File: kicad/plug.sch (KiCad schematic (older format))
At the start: 14 parts, among them J1 74320-1004

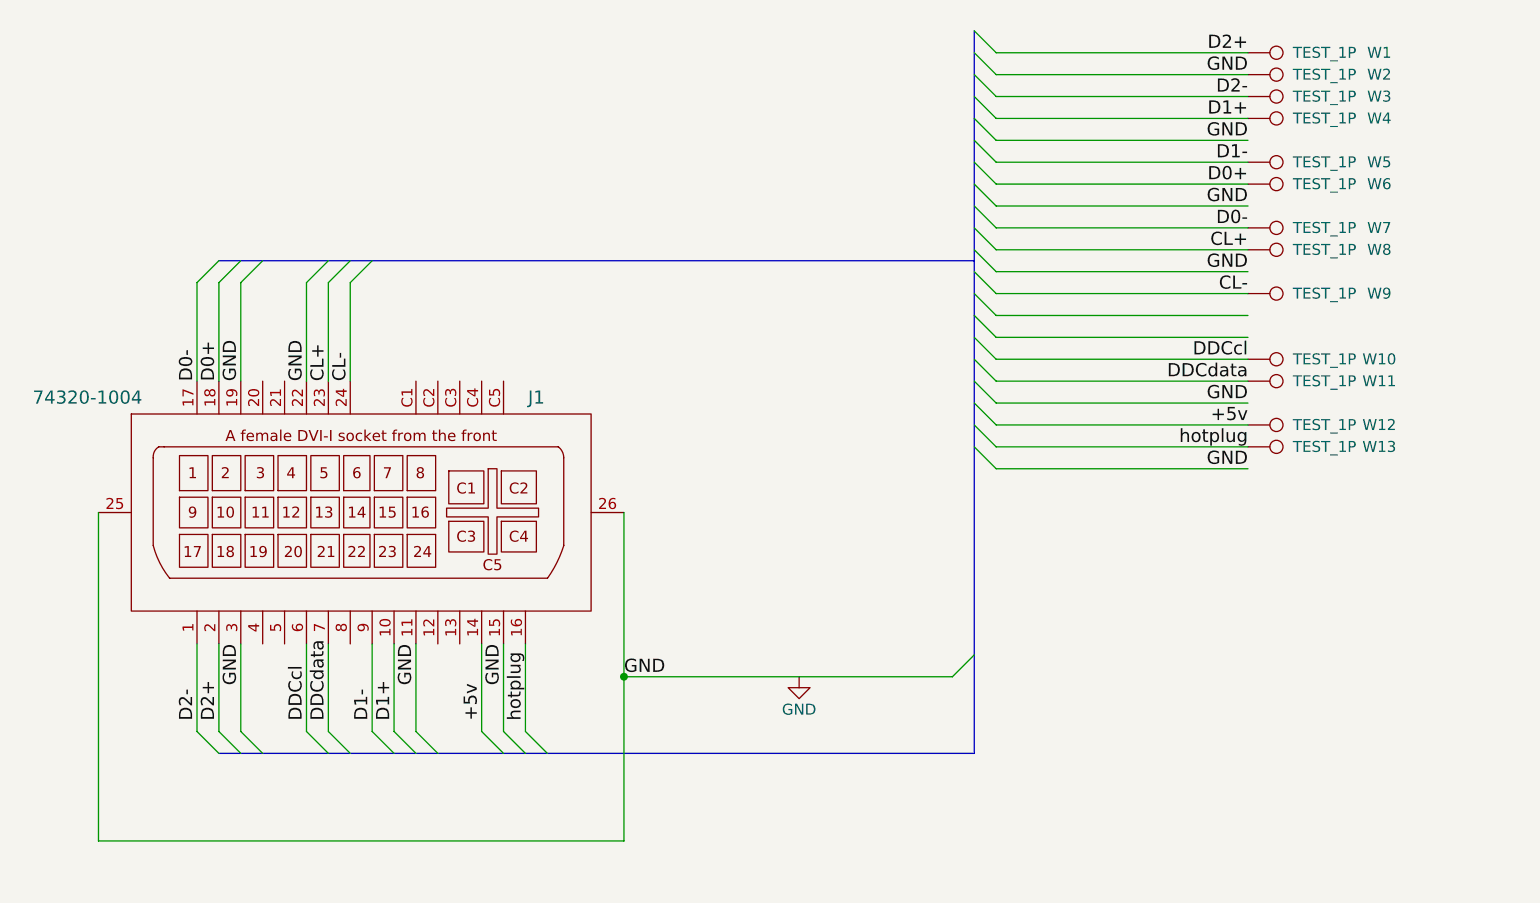
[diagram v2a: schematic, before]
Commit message: added pad footprint
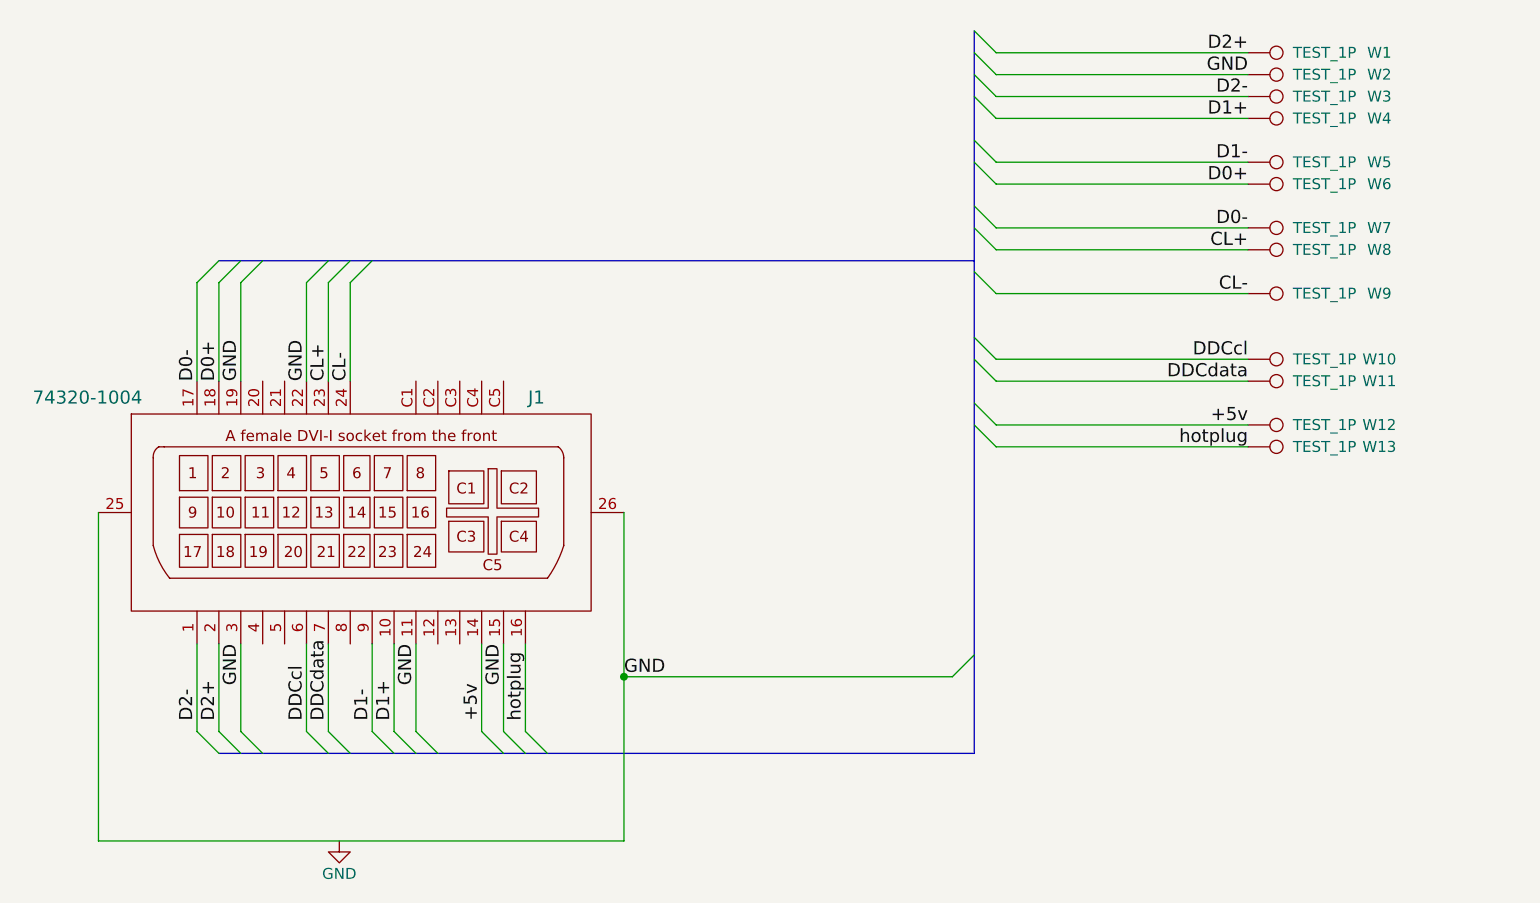
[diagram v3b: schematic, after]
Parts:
- W1, W10, W11, W12, W13, W2, W3, W4, W5, W6, W7, W8, W9: footprint Connectors:PINTST -> project:pad
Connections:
- wire segments 42 -> 35
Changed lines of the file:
@@
 	7700 3700 7800 3800
 Entry Wire Line
-	7700 3600 7800 3700
-Entry Wire Line
 	7700 3500 7800 3600
 Entry Wire Line
 	7700 3400 7800 3500
-Entry Wire Line
-	7700 3300 7800 3400
-Entry Wire Line
-	7700 3200 7800 3300
 Entry Wire Line
 	7700 3100 7800 3200
@@
 Text Label 4350 3600 1    60   ~ 0
 GND
-Entry Wire Line
-	7700 2700 7800 2800
-Text Label 8950 2800 2    60   ~ 0
-GND
-Entry Wire Line
-	7700 3000 7800 3100
-Text Label 8950 3100 2    60   ~ 0
-GND
 Wire Wire Line
 	6100 5700 3700 5700
@@
 	8950 3800 7800 3800
 Wire Wire Line
-	8950 3700 7800 3700
-Wire Wire Line
 	8950 3600 7800 3600
 Wire Wire Line
 	8950 3500 7800 3500
-Wire Wire Line
-	8950 3400 7800 3400
-Wire Wire Line
-	8950 3300 7800 3300
 Wire Wire Line
 	8950 3200 7800 3200
@@
 	4350 3600 4350 3150
 Wire Wire Line
-	7800 2800 8950 2800
-Wire Wire Line
-	7800 3100 8950 3100
-Wire Wire Line
 	4650 3600 4650 3150
 Entry Wire Line
@@
 	5150 5200 5250 5300
 Text Label 5150 4800 3    60   ~ 0
-GND
-Wire Wire Line
-	8950 2500 7800 2500
-Entry Wire Line
-	7700 2400 7800 2500
-Text Label 8950 2500 2    60   ~ 0
 GND
 Entry Wire Line
@@
 Connection ~ 6100 4950
 Text Label 6100 4950 0    60   ~ 0
-GND
-Entry Wire Line
-	7700 3900 7800 4000
-Wire Wire Line
-	7800 4000 8950 4000
-Text Label 8950 4000 2    60   ~ 0
-GND
-Text Label 8950 3700 2    60   ~ 0
 GND
 Entry Wire Line
@@
 F 0 "W1" V 8950 2700 50  0000 C CNN
 F 1 "TEST_1P" V 8950 2450 50  0000 C CNN
-F 2 "Connectors:PINTST" H 9150 2100 50  0001 C CNN
+F 2 "project:pad" H 9150 2100 50  0001 C CNN
 F 3 "" H 9150 2100 50  0000 C CNN
 	1    8950 2100
@@
 F 0 "W2" V 8950 2800 50  0000 C CNN
 F 1 "TEST_1P" V 8950 2550 50  0000 C CNN
-F 2 "Connectors:PINTST" H 9150 2200 50  0001 C CNN
+F 2 "project:pad" H 9150 2200 50  0001 C CNN
 F 3 "" H 9150 2200 50  0000 C CNN
 	1    8950 2200
@@
 F 0 "W3" V 8950 2900 50  0000 C CNN
 F 1 "TEST_1P" V 8950 2650 50  0000 C CNN
-F 2 "Connectors:PINTST" H 9150 2300 50  0001 C CNN
+F 2 "project:pad" H 9150 2300 50  0001 C CNN
 F 3 "" H 9150 2300 50  0000 C CNN
 	1    8950 2300
@@
 F 0 "W4" V 8950 3000 50  0000 C CNN
 F 1 "TEST_1P" V 8950 2750 50  0000 C CNN
-F 2 "Connectors:PINTST" H 9150 2400 50  0001 C CNN
+F 2 "project:pad" H 9150 2400 50  0001 C CNN
 F 3 "" H 9150 2400 50  0000 C CNN
 	1    8950 2400
@@
 F 0 "W5" V 8950 3200 50  0000 C CNN
 F 1 "TEST_1P" V 8950 2950 50  0000 C CNN
-F 2 "Connectors:PINTST" H 9150 2600 50  0001 C CNN
+F 2 "project:pad" H 9150 2600 50  0001 C CNN
 F 3 "" H 9150 2600 50  0000 C CNN
 	1    8950 2600
@@
 F 0 "W6" V 8950 3300 50  0000 C CNN
 F 1 "TEST_1P" V 8950 3050 50  0000 C CNN
-F 2 "Connectors:PINTST" H 9150 2700 50  0001 C CNN
+F 2 "project:pad" H 9150 2700 50  0001 C CNN
 F 3 "" H 9150 2700 50  0000 C CNN
 	1    8950 2700
@@
 F 0 "W7" V 8950 3500 50  0000 C CNN
 F 1 "TEST_1P" V 8950 3250 50  0000 C CNN
-F 2 "Connectors:PINTST" H 9150 2900 50  0001 C CNN
+F 2 "project:pad" H 9150 2900 50  0001 C CNN
 F 3 "" H 9150 2900 50  0000 C CNN
 	1    8950 2900
@@
 F 0 "W8" V 8950 3600 50  0000 C CNN
 F 1 "TEST_1P" V 8950 3350 50  0000 C CNN
-F 2 "Connectors:PINTST" H 9150 3000 50  0001 C CNN
+F 2 "project:pad" H 9150 3000 50  0001 C CNN
 F 3 "" H 9150 3000 50  0000 C CNN
 	1    8950 3000
@@
 F 0 "W9" V 8950 3800 50  0000 C CNN
 F 1 "TEST_1P" V 8950 3550 50  0000 C CNN
-F 2 "Connectors:PINTST" H 9150 3200 50  0001 C CNN
+F 2 "project:pad" H 9150 3200 50  0001 C CNN
 F 3 "" H 9150 3200 50  0000 C CNN
 	1    8950 3200
@@
 F 0 "W10" V 8950 4100 50  0000 C CNN
 F 1 "TEST_1P" V 8950 3850 50  0000 C CNN
-F 2 "Connectors:PINTST" H 9150 3500 50  0001 C CNN
+F 2 "project:pad" H 9150 3500 50  0001 C CNN
 F 3 "" H 9150 3500 50  0000 C CNN
 	1    8950 3500
@@
 F 0 "W11" V 8950 4200 50  0000 C CNN
 F 1 "TEST_1P" V 8950 3950 50  0000 C CNN
-F 2 "Connectors:PINTST" H 9150 3600 50  0001 C CNN
+F 2 "project:pad" H 9150 3600 50  0001 C CNN
 F 3 "" H 9150 3600 50  0000 C CNN
 	1    8950 3600
@@
 F 0 "W12" V 8950 4400 50  0000 C CNN
 F 1 "TEST_1P" V 8950 4150 50  0000 C CNN
-F 2 "Connectors:PINTST" H 9150 3800 50  0001 C CNN
+F 2 "project:pad" H 9150 3800 50  0001 C CNN
 F 3 "" H 9150 3800 50  0000 C CNN
 	1    8950 3800
@@
 F 0 "W13" V 8950 4500 50  0000 C CNN
 F 1 "TEST_1P" V 8950 4250 50  0000 C CNN
-F 2 "Connectors:PINTST" H 9150 3900 50  0001 C CNN
+F 2 "project:pad" H 9150 3900 50  0001 C CNN
 F 3 "" H 9150 3900 50  0000 C CNN
 	1    8950 3900
@@
 L GND #PWR01
 U 1 1 5855A718
-P 6900 4950
-F 0 "#PWR01" H 6900 4700 50  0001 C CNN
-F 1 "GND" H 6900 4800 50  0000 C CNN
-F 2 "" H 6900 4950 50  0000 C CNN
-F 3 "" H 6900 4950 50  0000 C CNN
-	1    6900 4950
+P 4800 5700
+F 0 "#PWR01" H 4800 5450 50  0001 C CNN
+F 1 "GND" H 4800 5550 50  0000 C CNN
+F 2 "" H 4800 5700 50  0000 C CNN
+F 3 "" H 4800 5700 50  0000 C CNN
+	1    4800 5700
 	1    0    0    -1
 $EndComp
